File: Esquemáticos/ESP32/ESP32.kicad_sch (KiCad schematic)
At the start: 4 parts

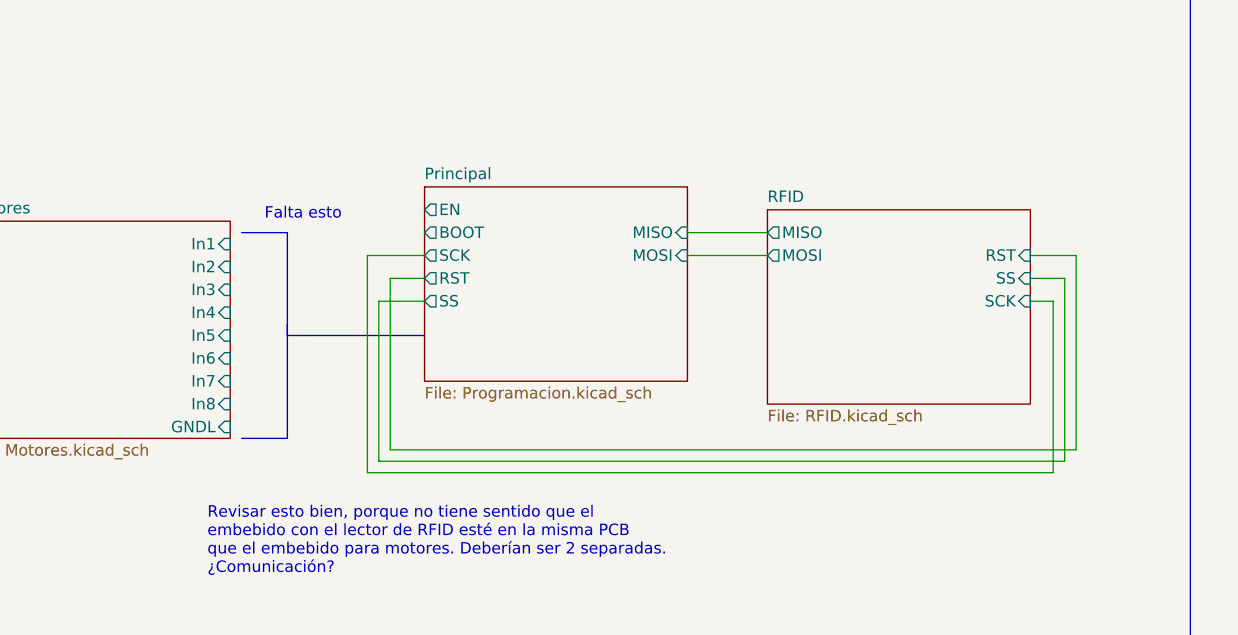
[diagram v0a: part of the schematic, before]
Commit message: Añadí las conexiones con los optoacopladores
Además arreglé la posición de algunas vías.
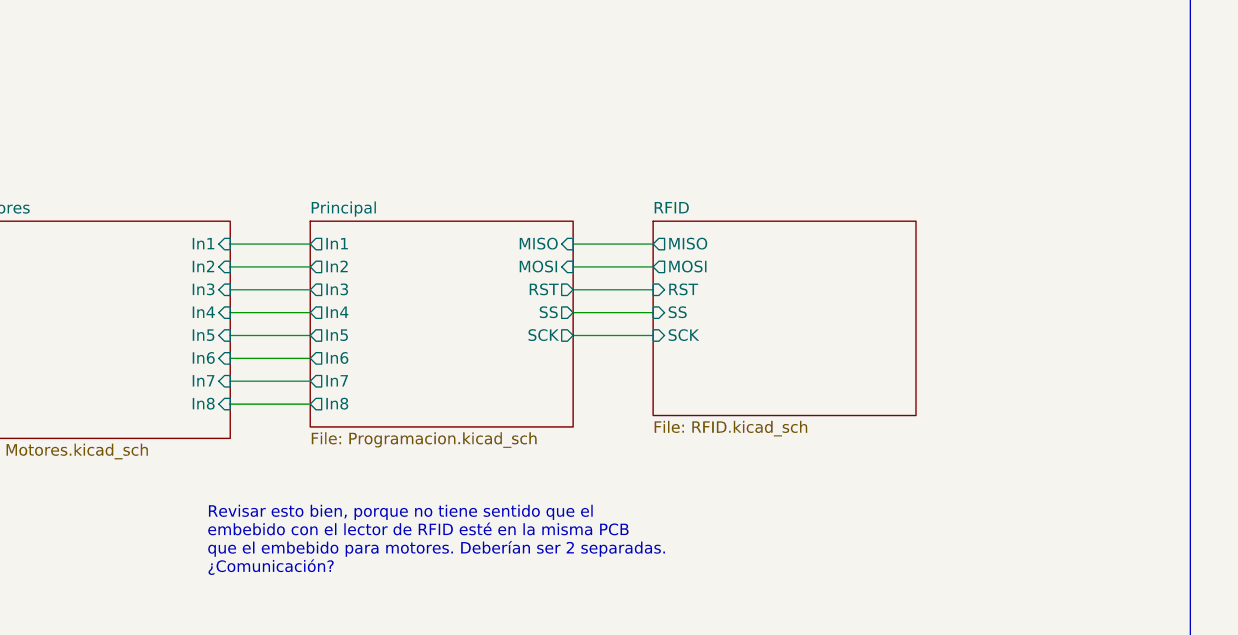
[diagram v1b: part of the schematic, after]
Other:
- sheet Motores ports: added none; removed GNDL
- sheet Principal ports: added In1, In2, In3, In4, In5, In6, In7, In8; removed BOOT, EN
- note removed: "Falta esto"

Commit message: Huellas actualizadas según los vendedores locales
Falta la del optoacoplador y actualizar la placa. Además, dependiendo de la resñpuesta del profe tocaría re-diseñar todo :c
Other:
- note removed: "Revisar esto bien, porque no tiene sentido que el embebido con el lector de RFID esté en la misma PCB que el embebido para motores. Deberían ser 2 separadas. ¿Comunicación?"
